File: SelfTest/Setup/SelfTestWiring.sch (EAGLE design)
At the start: 10 parts

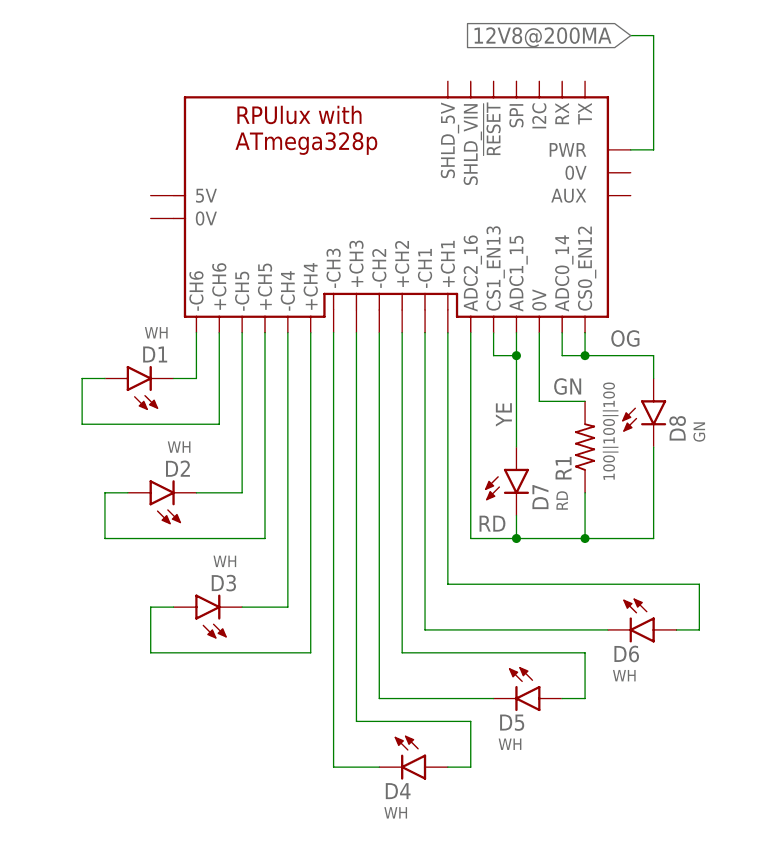
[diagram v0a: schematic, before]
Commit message: SelfTest: LED channels are running at half curr
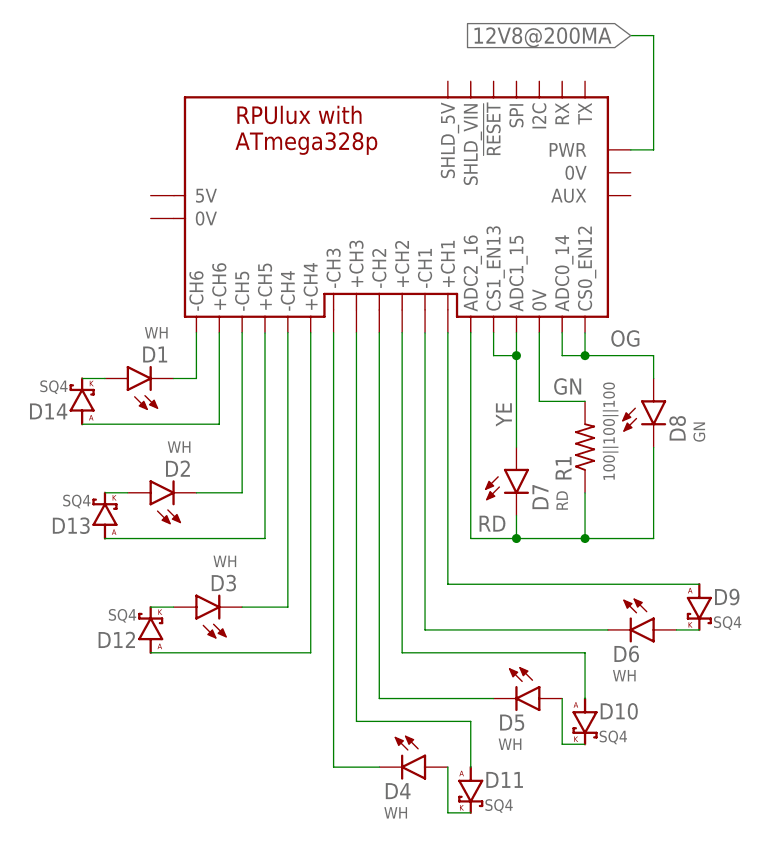
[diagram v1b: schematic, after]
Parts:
- added D10, D11, D12, D13, D14, D9: SQ4, D-SBR:DSMA
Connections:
- new net N$13: D6.A, D9.K
- new net N$14: D12.K, D3.A
- new net N$15: D13.K, D2.A
- new net N$16: D1.A, D14.K
- new net N$17: D10.K, D5.A
- new net N$18: D11.K, D4.A
- net N$10: now also D11.A; no longer D4.A
- net N$11: now also D10.A; no longer D5.A
- net N$12: now also D9.A; no longer D6.A
- net N$7: now also D14.A; no longer D1.A
- net N$8: now also D13.A; no longer D2.A
- net N$9: now also D12.A; no longer D3.A
